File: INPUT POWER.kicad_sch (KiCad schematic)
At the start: 20 parts, among them J1 TYPE-C-31-M12_13, SW3 ON/OFF, U3 IP5306

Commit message: Assigned PN and Footprint for C
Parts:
- added C36: 10uF, ESP32-S3_DB:C_0805_2012Metric, symbol ESP32-S3_DB:C
- C10, C9: footprint (none) -> ESP32-S3_DB:C_0805_2012Metric; PN (none) -> CL21A106KAYNNNE
- C28: footprint (none) -> ESP32-S3_DB:C_0603_1608Metric; PN (none) -> CL10A226MO7JZNC
- D1: footprint (none) -> ESP32-S3_DB:LED_0603_1608Metric; PN (none) -> NCD0603B1
- D2: footprint PRTR5V0U2X -> (none)
- D3, D7, D8, D9: footprint (none) -> ESP32-S3_DB:LED_0603_1608Metric; PN (none) -> NCD0603C1
- SW3: PN (none) -> K2-1187SQ-A4SW-06
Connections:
- net GND: now also C36.2
- net V_BAT: now also C36.1
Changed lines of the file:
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@@
   (junction (at 238.76 72.39) (diameter 0) (color 0 0 0 0)
+  )
+  (junction (at 238.76 83.82) (diameter 0) (color 0 0 0 0)
   )
   (junction (at 130.81 59.055) (diameter 0) (color 0 0 0 0)
@@
     (stroke (width 0) (type default))
   )
+  (wire (pts (xy 245.745 83.82) (xy 245.745 82.55))
+    (stroke (width 0) (type default))
+  )
   (bus (pts (xy 45.085 45.72) (xy 45.085 135.255))
     (stroke (width 1) (type default) (color 72 72 72 1))
@@
     (stroke (width 0) (type default))
   )
+  (wire (pts (xy 245.745 72.39) (xy 245.745 74.93))
+    (stroke (width 0) (type default))
+  )
   (bus (pts (xy 251.46 107.315) (xy 164.465 107.315))
     (stroke (width 1) (type default) (color 72 72 72 1))
@@
     (stroke (width 0) (type default))
   )
+  (wire (pts (xy 238.76 72.39) (xy 245.745 72.39))
+    (stroke (width 0) (type default))
+  )
   (wire (pts (xy 200.66 92.075) (xy 202.565 92.075))
     (stroke (width 0) (type default))
@@
     (stroke (width 0) (type default))
   )
-  (wire (pts (xy 238.76 84.455) (xy 238.76 82.55))
+  (wire (pts (xy 238.76 84.455) (xy 238.76 83.82))
     (stroke (width 0) (type default))
   )
@@
     (stroke (width 0) (type default))
   )
+  (wire (pts (xy 238.76 83.82) (xy 245.745 83.82))
+    (stroke (width 0) (type default))
+  )
   (wire (pts (xy 189.865 74.93) (xy 194.945 74.93))
     (stroke (width 0) (type default))
@@
   )
   (wire (pts (xy 106.68 127) (xy 104.14 127))
+    (stroke (width 0) (type default))
+  )
+  (wire (pts (xy 238.76 83.82) (xy 238.76 82.55))
     (stroke (width 0) (type default))
   )
@@
       (effects (font (size 1.27 1.27)) (justify left))
     )
-    (property "Footprint" "" (at 206.375 88.265 0)
+    (property "Footprint" "ESP32-S3_DB:LED_0603_1608Metric" (at 206.375 88.265 0)
       (effects (font (size 1.27 1.27)) hide)
     )
     (property "Datasheet" "~" (at 206.375 88.265 0)
+      (effects (font (size 1.27 1.27)) hide)
+    )
+    (property "PN" "NCD0603C1" (at 206.375 88.265 0)
       (effects (font (size 1.27 1.27)) hide)
     )
@@
       (effects (font (size 1.27 1.27)))
     )
-    (property "Footprint" "PRTR5V0U2X" (at 85.09 186.995 0)
+    (property "Footprint" "" (at 85.09 186.995 0)
       (effects (font (size 1.27 1.27)) (justify left top) hide)
     )
@@
       (effects (font (size 1.27 1.27)) (justify left))
     )
-    (property "Footprint" "" (at 174.9552 83.82 0)
+    (property "Footprint" "ESP32-S3_DB:C_0805_2012Metric" (at 174.9552 83.82 0)
       (effects (font (size 1.27 1.27)) hide)
     )
     (property "Datasheet" "~" (at 173.99 80.01 0)
+      (effects (font (size 1.27 1.27)) hide)
+    )
+    (property "PN" "CL21A106KAYNNNE" (at 173.99 80.01 0)
       (effects (font (size 1.27 1.27)) hide)
     )
@@
       (effects (font (size 1.27 1.27)) (justify left))
     )
-    (property "Footprint" "" (at 239.7252 82.55 0)
+    (property "Footprint" "ESP32-S3_DB:C_0603_1608Metric" (at 239.7252 82.55 0)
       (effects (font (size 1.27 1.27)) hide)
     )
@@
       (effects (font (size 1.27 1.27)) hide)
     )
+    (property "PN" "CL10A226MO7JZNC" (at 238.76 78.74 0)
+      (effects (font (size 1.27 1.27)) hide)
+    )
     (pin "1")
     (pin "2")
@@
       (effects (font (size 1.27 1.27)) (justify left))
     )
-    (property "Footprint" "" (at 206.375 92.075 0)
+    (property "Footprint" "ESP32-S3_DB:LED_0603_1608Metric" (at 206.375 92.075 0)
       (effects (font (size 1.27 1.27)) hide)
     )
@@
       (effects (font (size 1.27 1.27)) hide)
     )
+    (property "PN" "NCD0603C1" (at 206.375 92.075 0)
+      (effects (font (size 1.27 1.27)) hide)
+    )
     (pin "1")
     (pin "2")
@@
       (effects (font (size 1.27 1.27)) hide)
     )
+    (property "PN" "K2-1187SQ-A4SW-06" (at 227.33 81.28 0)
+      (effects (font (size 1.27 1.27)) hide)
+    )
     (pin "1")
     (pin "2")
@@
       (effects (font (size 1.27 1.27)) (justify left))
     )
-    (property "Footprint" "" (at 183.2102 79.375 0)
+    (property "Footprint" "ESP32-S3_DB:C_0805_2012Metric" (at 183.2102 79.375 0)
       (effects (font (size 1.27 1.27)) hide)
     )
@@
       (effects (font (size 1.27 1.27)) hide)
     )
+    (property "PN" "CL21A106KAYNNNE" (at 182.245 75.565 0)
+      (effects (font (size 1.27 1.27)) hide)
+    )
     (pin "1")
     (pin "2")
@@
       (effects (font (size 1.27 1.27)) (justify left))
     )
-    (property "Footprint" "" (at 206.375 100.965 0)
+    (property "Footprint" "ESP32-S3_DB:LED_0603_1608Metric" (at 206.375 100.965 0)
       (effects (font (size 1.27 1.27)) hide)
     )
@@
       (effects (font (size 1.27 1.27)) hide)
     )
+    (property "PN" "NCD0603C1" (at 206.375 100.965 0)
+      (effects (font (size 1.27 1.27)) hide)
+    )
     (pin "1")
     (pin "2")
@@
     )
   )
+  (symbol (lib_id "ESP32-S3_DB:C") (at 245.745 78.74 0) (unit 1)
+    (in_bom yes) (on_board yes) (dnp no)
+    (property "Reference" "C36" (at 241.3 76.835 0)
+      (effects (font (size 1.27 1.27)) (justify left))
+    )
+    (property "Value" "10uF" (at 246.38 80.645 0)
+      (effects (font (size 1.27 1.27)) (justify left))
+    )
+    (property "Footprint" "ESP32-S3_DB:C_0805_2012Metric" (at 246.7102 82.55 0)
+      (effects (font (size 1.27 1.27)) hide)
+    )
+    (property "Datasheet" "~" (at 245.745 78.74 0)
+      (effects (font (size 1.27 1.27)) hide)
+    )
+    (property "PN" "CL21A106KAYNNNE" (at 245.745 78.74 0)
+      (effects (font (size 1.27 1.27)) hide)
+    )
+    (pin "1")
+    (pin "2")
+    (instances
+      (project "ESP32-S3_DB"
+        (path "/b7fc4bd3-c219-4455-832b-8d795385dcf1/95090a63-7b3c-4ea0-92b8-aeafe05264cd"
+          (reference "C36") (unit 1)
+        )
+      )
+    )
+  )
   (symbol (lib_id "ESP32-S3_DB:L") (at 228.6 69.85 90) (unit 1)
     (in_bom yes) (on_board yes) (dnp no)
@@
       (effects (font (size 1.27 1.27)) (justify left))
     )
-    (property "Footprint" "" (at 206.375 96.52 0)
+    (property "Footprint" "ESP32-S3_DB:LED_0603_1608Metric" (at 206.375 96.52 0)
       (effects (font (size 1.27 1.27)) hide)
     )
     (property "Datasheet" "~" (at 206.375 96.52 0)
+      (effects (font (size 1.27 1.27)) hide)
+    )
+    (property "PN" "NCD0603C1" (at 206.375 96.52 0)
       (effects (font (size 1.27 1.27)) hide)
     )
@@
       (effects (font (size 1.27 1.27)) (justify right))
     )
-    (property "Footprint" "" (at 62.865 65.405 0)
+    (property "Footprint" "ESP32-S3_DB:LED_0603_1608Metric" (at 62.865 65.405 0)
       (effects (font (size 1.27 1.27)) hide)
     )
@@
       (effects (font (size 1.27 1.27)) hide)
     )
+    (property "PN" "NCD0603B1" (at 62.865 65.405 0)
+      (effects (font (size 1.27 1.27)) hide)
+    )

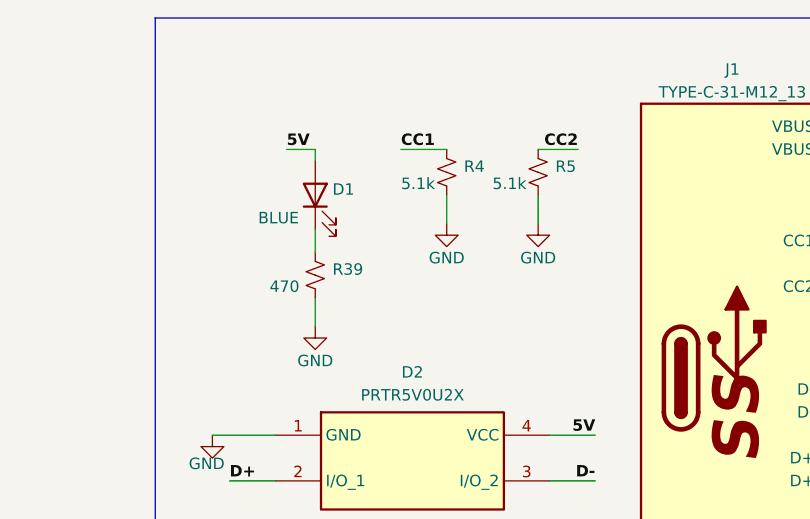
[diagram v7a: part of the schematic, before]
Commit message: Assigned footprints
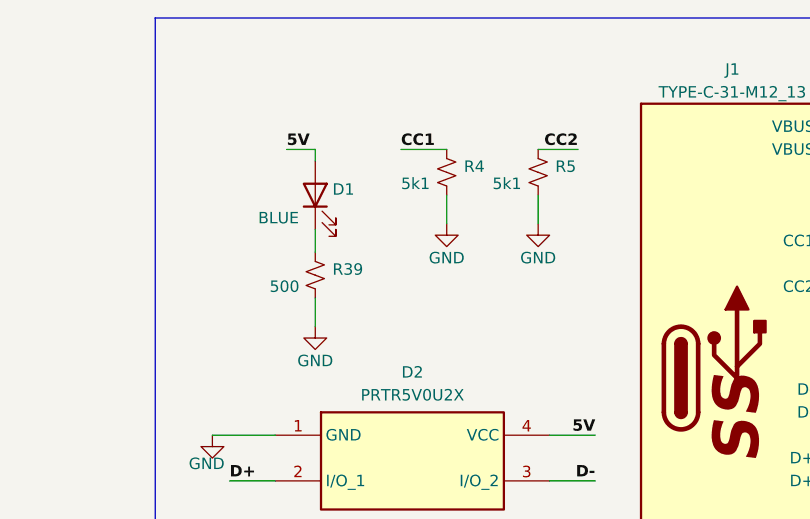
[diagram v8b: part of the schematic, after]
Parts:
- C10, C36, C9: footprint ESP32-S3_DB:C_0805_2012Metric -> ESP32-S3_Dev_Board:C_0805_2012Metric
- C28: footprint ESP32-S3_DB:C_0603_1608Metric -> ESP32-S3_Dev_Board:C_0603_1608Metric
- D2: footprint (none) -> ESP32-S3_Dev_Board:SOT-143
- D3, D7, D8, D9: footprint ESP32-S3_DB:LED_0603_1608Metric -> ESP32-S3_Dev_Board:LED_0603_1608Metric
- J1: footprint acheron_Connectors:TYPE-C-31-M-12 -> ESP32-S3_Dev_Board:USB-C_SMD-TYPE-C-31-M-12
- R10: footprint (none) -> ESP32-S3_Dev_Board:R_0402_1005Metric; PN (none) -> CSR0402FKR500
- R15, R16: footprint (none) -> ESP32-S3_Dev_Board:R_0603_1608Metric; PN (none) -> RC0603JR-070RL
- R39: value 470 -> 500; footprint (none) -> ESP32-S3_Dev_Board:R_0402_1005Metric; PN (none) -> RC0402FR-07499RL
- R4, R5: value 5.1k -> 5k1; footprint (none) -> ESP32-S3_Dev_Board:R_0402_1005Metric; PN (none) -> RC0402FR-075K1L
- R9: footprint (none) -> ESP32-S3_Dev_Board:R_0402_1005Metric; PN (none) -> RC0402JR-072RL
- SW3: footprint (none) -> ESP32-S3_Dev_Board:KEY-SMD_4P-L5.2-W5.2-P3.70-LS6.4
- U3: footprint easyeda2kicad:ESOP-8_L4.9-W3.9-P1.27-LS6.0-BL-EP -> ESP32-S3_Dev_Board:ESOP-8_L4.9-W3.9-P1.27-LS6.0-BL-EP
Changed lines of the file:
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@@
       (effects (font (size 1.27 1.27)) (justify left))
     )
-    (property "Footprint" "" (at 224.155 67.31 0)
+    (property "Footprint" "ESP32-S3_Dev_Board:R_0603_1608Metric" (at 224.155 67.31 0)
       (effects (font (size 1.27 1.27)) hide)
     )
@@
       (effects (font (size 1.27 1.27)) hide)
     )
+    (property "PN" "RC0603JR-070RL" (at 224.155 67.31 0)
+      (effects (font (size 1.27 1.27)) hide)
+    )
     (pin "1")
     (pin "2")
@@
       (effects (font (size 1.27 1.27)) (justify left))
     )
-    (property "Footprint" "ESP32-S3_DB:LED_0603_1608Metric" (at 206.375 88.265 0)
+    (property "Footprint" "ESP32-S3_Dev_Board:LED_0603_1608Metric" (at 206.375 88.265 0)
       (effects (font (size 1.27 1.27)) hide)
     )
@@
       (effects (font (size 1.27 1.27)))
     )
-    (property "Footprint" "" (at 85.09 186.995 0)
+    (property "Footprint" "ESP32-S3_Dev_Board:SOT-143" (at 85.09 186.995 0)
       (effects (font (size 1.27 1.27)) (justify left top) hide)
     )
@@
       (effects (font (size 1.27 1.27)) (justify left))
     )
-    (property "Footprint" "ESP32-S3_DB:C_0805_2012Metric" (at 174.9552 83.82 0)
+    (property "Footprint" "ESP32-S3_Dev_Board:C_0805_2012Metric" (at 174.9552 83.82 0)
       (effects (font (size 1.27 1.27)) hide)
     )
@@
       (effects (font (size 1.27 1.27)) (justify left))
     )
-    (property "Value" "470" (at 57.785 75.565 0)
-      (effects (font (size 1.27 1.27)) (justify left))
-    )
-    (property "Footprint" "" (at 62.865 74.295 0)
+    (property "Value" "500" (at 57.785 75.565 0)
+      (effects (font (size 1.27 1.27)) (justify left))
+    )
+    (property "Footprint" "ESP32-S3_Dev_Board:R_0402_1005Metric" (at 62.865 74.295 0)
       (effects (font (size 1.27 1.27)) hide)
     )
     (property "Datasheet" "~" (at 62.865 74.295 0)
+      (effects (font (size 1.27 1.27)) hide)
+    )
+    (property "PN" "RC0402FR-07499RL" (at 62.865 74.295 0)
       (effects (font (size 1.27 1.27)) hide)
     )
@@
       (effects (font (size 1.27 1.27)))
     )
-    (property "Footprint" "easyeda2kicad:ESOP-8_L4.9-W3.9-P1.27-LS6.0-BL-EP" (at 207.645 82.55 0)
+    (property "Footprint" "ESP32-S3_Dev_Board:ESOP-8_L4.9-W3.9-P1.27-LS6.0-BL-EP" (at 207.645 82.55 0)
       (effects (font (size 1.27 1.27)) hide)
     )
@@
       (effects (font (size 1.27 1.27)) (justify left))
     )
-    (property "Footprint" "ESP32-S3_DB:C_0603_1608Metric" (at 239.7252 82.55 0)
+    (property "Footprint" "ESP32-S3_Dev_Board:C_0603_1608Metric" (at 239.7252 82.55 0)
       (effects (font (size 1.27 1.27)) hide)
     )
@@
       (effects (font (size 1.27 1.27)) (justify left))
     )
-    (property "Footprint" "ESP32-S3_DB:LED_0603_1608Metric" (at 206.375 92.075 0)
+    (property "Footprint" "ESP32-S3_Dev_Board:LED_0603_1608Metric" (at 206.375 92.075 0)
       (effects (font (size 1.27 1.27)) hide)
     )
@@
       (effects (font (size 1.27 1.27)) (justify left))
     )
-    (property "Footprint" "" (at 228.6 72.39 0)
+    (property "Footprint" "ESP32-S3_Dev_Board:R_0402_1005Metric" (at 228.6 72.39 0)
       (effects (font (size 1.27 1.27)) hide)
     )
@@
       (effects (font (size 1.27 1.27)) hide)
     )
+    (property "PN" "CSR0402FKR500" (at 228.6 72.39 0)
+      (effects (font (size 1.27 1.27)) hide)
+    )
     (pin "1")
     (pin "2")
@@
       (effects (font (size 1.27 1.27)))
     )
-    (property "Footprint" "" (at 227.33 76.2 0)
+    (property "Footprint" "ESP32-S3_Dev_Board:KEY-SMD_4P-L5.2-W5.2-P3.70-LS6.4" (at 227.33 76.2 0)
       (effects (font (size 1.27 1.27)) hide)
     )
@@
       (effects (font (size 1.27 1.27)) (justify left))
     )
-    (property "Footprint" "ESP32-S3_DB:C_0805_2012Metric" (at 183.2102 79.375 0)
+    (property "Footprint" "ESP32-S3_Dev_Board:C_0805_2012Metric" (at 183.2102 79.375 0)
       (effects (font (size 1.27 1.27)) hide)
     )
@@
       (effects (font (size 1.27 1.27)) (justify left))
     )
-    (property "Value" "5.1k" (at 72.39 64.135 0)
-      (effects (font (size 1.27 1.27)) (justify left))
-    )
-    (property "Footprint" "" (at 77.47 62.865 0)
+    (property "Value" "5k1" (at 72.39 64.135 0)
+      (effects (font (size 1.27 1.27)) (justify left))
+    )
+    (property "Footprint" "ESP32-S3_Dev_Board:R_0402_1005Metric" (at 77.47 62.865 0)
       (effects (font (size 1.27 1.27)) hide)
     )
@@
       (effects (font (size 1.27 1.27)) hide)
     )
+    (property "PN" "RC0402FR-075K1L" (at 77.47 62.865 0)
+      (effects (font (size 1.27 1.27)) hide)
+    )
     (pin "1")
     (pin "2")
@@
       (effects (font (size 1.27 1.27)) (justify left))
     )
-    (property "Value" "5.1k" (at 82.55 64.135 0)
-      (effects (font (size 1.27 1.27)) (justify left))
-    )
-    (property "Footprint" "" (at 87.63 62.865 0)
+    (property "Value" "5k1" (at 82.55 64.135 0)
+      (effects (font (size 1.27 1.27)) (justify left))
+    )
+    (property "Footprint" "ESP32-S3_Dev_Board:R_0402_1005Metric" (at 87.63 62.865 0)
       (effects (font (size 1.27 1.27)) hide)
     )
@@
       (effects (font (size 1.27 1.27)) hide)
     )
+    (property "PN" "RC0402FR-075K1L" (at 87.63 62.865 0)
+      (effects (font (size 1.27 1.27)) hide)
+    )
     (pin "1")
     (pin "2")
@@
       (effects (font (size 1.27 1.27)) (justify left))
     )
-    (property "Footprint" "ESP32-S3_DB:LED_0603_1608Metric" (at 206.375 100.965 0)
+    (property "Footprint" "ESP32-S3_Dev_Board:LED_0603_1608Metric" (at 206.375 100.965 0)
       (effects (font (size 1.27 1.27)) hide)
     )
@@
       (effects (font (size 1.27 1.27)) (justify left))
     )
-    (property "Footprint" "ESP32-S3_DB:C_0805_2012Metric" (at 246.7102 82.55 0)
+    (property "Footprint" "ESP32-S3_Dev_Board:C_0805_2012Metric" (at 246.7102 82.55 0)
       (effects (font (size 1.27 1.27)) hide)
     )
@@
       (effects (font (size 1.27 1.27)) (justify left))
     )
-    (property "Footprint" "ESP32-S3_DB:LED_0603_1608Metric" (at 206.375 96.52 0)
+    (property "Footprint" "ESP32-S3_Dev_Board:LED_0603_1608Metric" (at 206.375 96.52 0)
       (effects (font (size 1.27 1.27)) hide)
     )
@@
       (effects (font (size 1.27 1.27)))
     )
-    (property "Footprint" "acheron_Connectors:TYPE-C-31-M-12" (at 96.52 85.725 90)
+    (property "Footprint" "ESP32-S3_Dev_Board:USB-C_SMD-TYPE-C-31-M-12" (at 96.52 85.725 90)
       (effects (font (size 1.27 1.27)) hide)
     )
@@
       (effects (font (size 1.27 1.27)) (justify left))
     )
-    (property "Footprint" "" (at 178.435 67.31 0)
+    (property "Footprint" "ESP32-S3_Dev_Board:R_0603_1608Metric" (at 178.435 67.31 0)
       (effects (font (size 1.27 1.27)) hide)
     )
     (property "Datasheet" "~" (at 178.435 67.31 0)
+      (effects (font (size 1.27 1.27)) hide)
+    )
+    (property "PN" "RC0603JR-070RL" (at 178.435 67.31 0)
       (effects (font (size 1.27 1.27)) hide)
     )
@@
       (effects (font (size 1.27 1.27)) (justify left))
     )
-    (property "Footprint" "" (at 173.99 71.755 0)
+    (property "Footprint" "ESP32-S3_Dev_Board:R_0402_1005Metric" (at 173.99 71.755 0)
       (effects (font (size 1.27 1.27)) hide)
     )
@@
       (effects (font (size 1.27 1.27)) hide)
     )
+    (property "PN" "RC0402JR-072RL" (at 173.99 71.755 0)
+      (effects (font (size 1.27 1.27)) hide)
+    )
